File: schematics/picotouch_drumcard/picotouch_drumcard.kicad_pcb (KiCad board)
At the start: 2 copper layers, 88.9 x 63.5 mm, 79 parts, among them J1 AudioJack4, J2 AudioJack4, J3 AudioJack4, SW1 Capacitive Button, SW10 Capacitive Button, SW11 Capacitive Button, SW12 Capacitive Button, SW13 Capacitive Button, SW14 Capacitive Button, SW15 Capacitive Button, SW16 Capacitive Button, SW17 Capacitive Button, SW18 SSSS811101, SW2 Capacitive Button, SW3 Capacitive Button, SW4 Capacitive Button, SW5 Capacitive Button, SW6 Capacitive Button, SW7 Capacitive Button, SW8 Capacitive Button, SW9 Capacitive Button, U1 Pico, U2 H11L1S(TA), U3 MCP73831-2-OT, U4 TS20, X1 AFC20-S02ACA-00

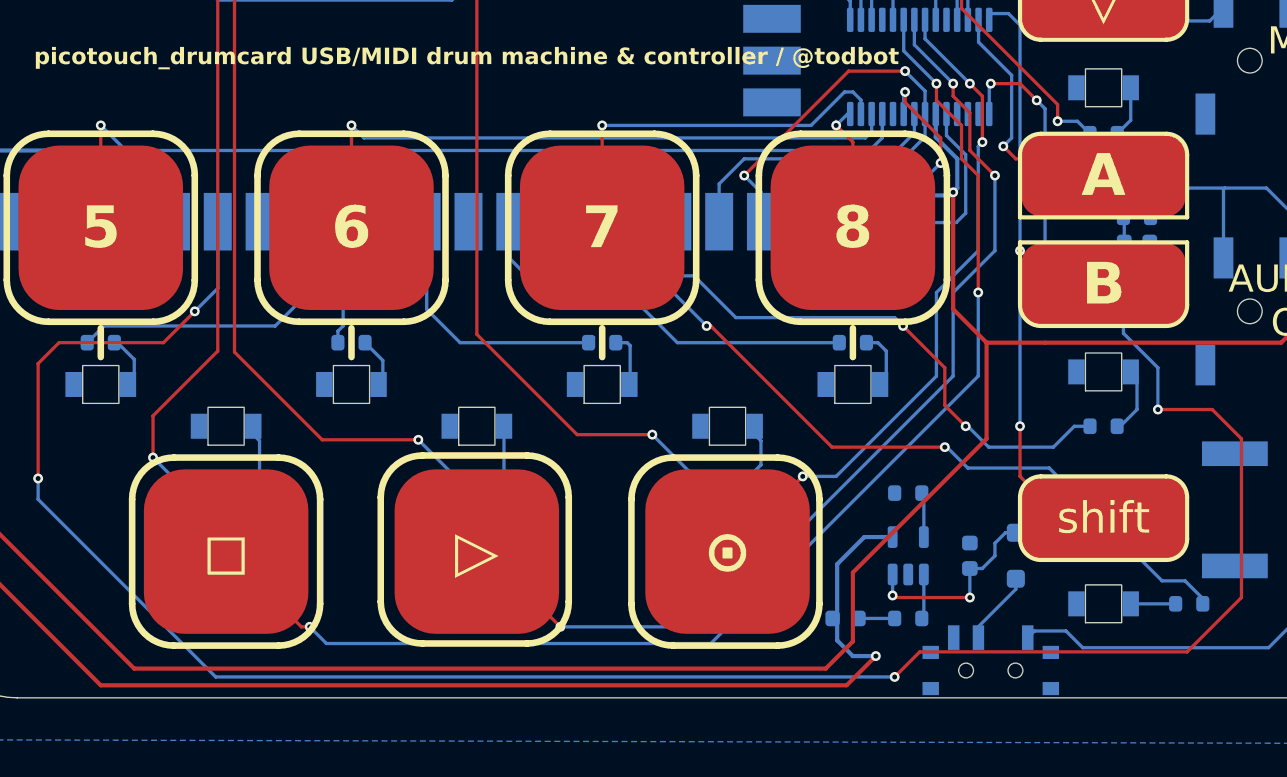
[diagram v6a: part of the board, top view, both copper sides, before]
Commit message: add missing cap to charger circuit, nudge around charger to fit
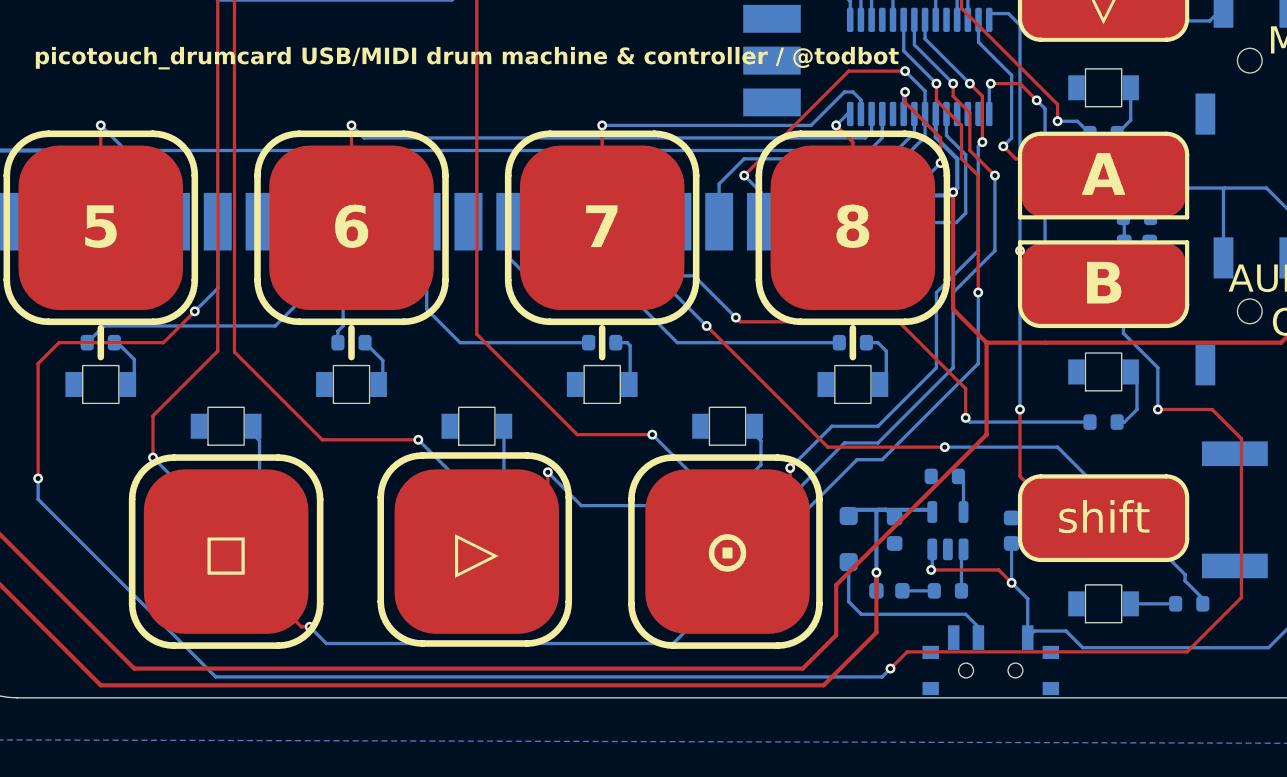
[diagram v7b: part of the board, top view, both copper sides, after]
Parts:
- added C6: 10uF, Capacitor_SMD:C_0603_1608Metric, B.Cu at (160.0, 66.0)
- moved D18 10.2 mm to (157.2, 66.5)
- moved D17 3.15 mm to (159.7, 69.7)
- moved C4 2.96 mm to (167.1, 66.0)
- moved R26 2.94 mm to (163.3, 69.7)
- moved U3 2.85 mm to (163.3, 66.0)
- moved R25 2.44 mm to (163.1, 62.7)
- moved R14 0.25 mm to (172.7, 59.4)
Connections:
- C4 pad 1: Net-(D18-K) -> +BATT
- D18 pad 1: Net-(D18-K) -> +5V
- SW18 pad 3: (no net) -> unconnected-(SW18-Pad3)
- U3 pad 3: Net-(D18-K) -> +BATT
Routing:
- net +BATT: track 26.2 -> 38.8 mm, vias 0 -> 2
- net Net-(D18-K): track 11.9 -> 0.00 mm, vias 2 -> 0
- net Net-(D18-A): track 4.52 -> 12.2 mm
- net +5V: track 91.7 -> 96.1 mm
- net /TOUCH10: track 62.3 -> 60.5 mm
- net /LED14: track 39.9 -> 38.5 mm
- net +3.3V: track 227.4 -> 226.6 mm

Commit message: sigh more fixes to charging circuit
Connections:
- U1 pad 39: unconnected-(U1-VSYS-Pad39) -> +5V
- U1 pad 40: +5V -> unconnected-(U1-VBUS-Pad40)
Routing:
- net +5V: track 96.1 -> 102.1 mm
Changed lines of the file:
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@@
 	(net 33 "/LED11")
 	(net 34 "unconnected-(U1-SWDIO-Pad43)")
-	(net 35 "unconnected-(U1-VSYS-Pad39)")
+	(net 35 "unconnected-(U1-VBUS-Pad40)")
 	(net 36 "unconnected-(U1-SWCLK-Pad41)")
 	(net 37 "unconnected-(U1-RUN-Pad30)")
@@
 			)
 			(layers "B.Cu" "B.Mask")
-			(net 35 "unconnected-(U1-VSYS-Pad39)")
+			(net 62 "+5V")
 			(pinfunction "VSYS")
-			(pintype "power_in+no_connect")
+			(pintype "power_in")
 		)
 		(pad "40" smd rect
@@
 			)
 			(layers "B.Cu" "B.Mask")
-			(net 62 "+5V")
+			(net 35 "unconnected-(U1-VBUS-Pad40)")
 			(pinfunction "VBUS")
-			(pintype "power_in")
+			(pintype "power_in+no_connect")
 		)
 		(pad "41" smd rect
@@
 	)
 	(segment
-		(start 154.432 74.422)
-		(end 113.792 74.422)
-		(width 0.254)
-		(layer "F.Cu")
-		(net 11)
-	)
-	(segment
-		(start 165.608 54.61)
-		(end 165.608 60.198)
+		(start 105.156 65.786)
+		(end 105.156 42.926)
 		(width 0.254)
 		(layer "F.Cu")
@@
 	)
 	(segment
-		(start 156.464 69.342)
-		(end 156.464 72.39)
+		(start 156.464 72.39)
+		(end 154.432 74.422)
 		(width 0.254)
 		(layer "F.Cu")
@@
 	)
 	(segment
-		(start 156.464 72.39)
-		(end 154.432 74.422)
+		(start 165.608 60.198)
+		(end 156.464 69.342)
 		(width 0.254)
 		(layer "F.Cu")
@@
 	)
 	(segment
-		(start 105.156 65.786)
-		(end 105.156 42.926)
+		(start 113.792 74.422)
+		(end 105.156 65.786)
 		(width 0.254)
 		(layer "F.Cu")
@@
 	)
 	(segment
-		(start 165.608 60.198)
-		(end 156.464 69.342)
-		(width 0.254)
-		(layer "F.Cu")
-		(net 11)
-	)
-	(segment
 		(start 185.42 52.705)
 		(end 185.42 15.24)
@@
 	)
 	(segment
+		(start 165.608 54.61)
+		(end 165.608 60.198)
+		(width 0.254)
+		(layer "F.Cu")
+		(net 11)
+	)
+	(segment
+		(start 154.432 74.422)
+		(end 113.792 74.422)
+		(width 0.254)
+		(layer "F.Cu")
+		(net 11)
+	)
+	(segment
 		(start 184.404 14.224)
 		(end 182.118 14.224)
@@
 	)
 	(segment
-		(start 113.792 74.422)
-		(end 105.156 65.786)
+		(start 156.464 69.342)
+		(end 156.464 72.39)
 		(width 0.254)
 		(layer "F.Cu")
@@
 	)
 	(segment
-		(start 103.632 67.31)
-		(end 103.632 52.07)
+		(start 158.912498 72.227502)
+		(end 158.912498 68.58)
 		(width 0.254)
 		(layer "F.Cu")
@@
 	(segment
 		(start 111.76 75.438)
-		(end 103.632 67.31)
+		(end 155.702 75.438)
 		(width 0.254)
 		(layer "F.Cu")
@@
 	)
 	(segment
-		(start 158.912498 68.58)
+		(start 155.702 75.438)
 		(end 158.912498 72.227502)
 		(width 0.254)
@@
 	)
 	(segment
-		(start 158.912498 72.227502)
-		(end 155.702 75.438)
+		(start 103.632 44.45)
+		(end 103.632 67.31)
 		(width 0.254)
 		(layer "F.Cu")
@@
 	)
 	(segment
-		(start 155.702 75.438)
+		(start 103.632 67.31)
 		(end 111.76 75.438)
 		(width 0.254)
@@
 	)
 	(via
-		(at 103.632 52.07)
+		(at 103.632 44.45)
 		(size 0.6)
 		(drill 0.3)
@@
 	)
 	(segment
-		(start 103.632 46.355)
-		(end 103.632 52.07)
+		(start 159.525 64.77)
+		(end 157.604001 64.77)
 		(width 0.254)
 		(layer "B.Cu")
@@
 	)
 	(segment
-		(start 159.525 64.77)
-		(end 157.604001 64.77)
+		(start 103.632 44.45)
+		(end 105.6 44.45)
+		(width 0.254)
+		(layer "B.Cu")
+		(net 62)
+	)
+	(segment
+		(start 105.6 44.45)
+		(end 106.172 45.022)
 		(width 0.254)
 		(layer "B.Cu")
@@
 		(width 0.254)
 		(layer "B.Cu")
+		(net 62)
+	)
+	(segment
+		(start 106.172 45.022)
+		(end 106.172 46.355)
+		(width 0.254)
+		(layer "B.Cu")
